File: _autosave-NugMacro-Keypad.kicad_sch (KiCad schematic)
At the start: 16 parts

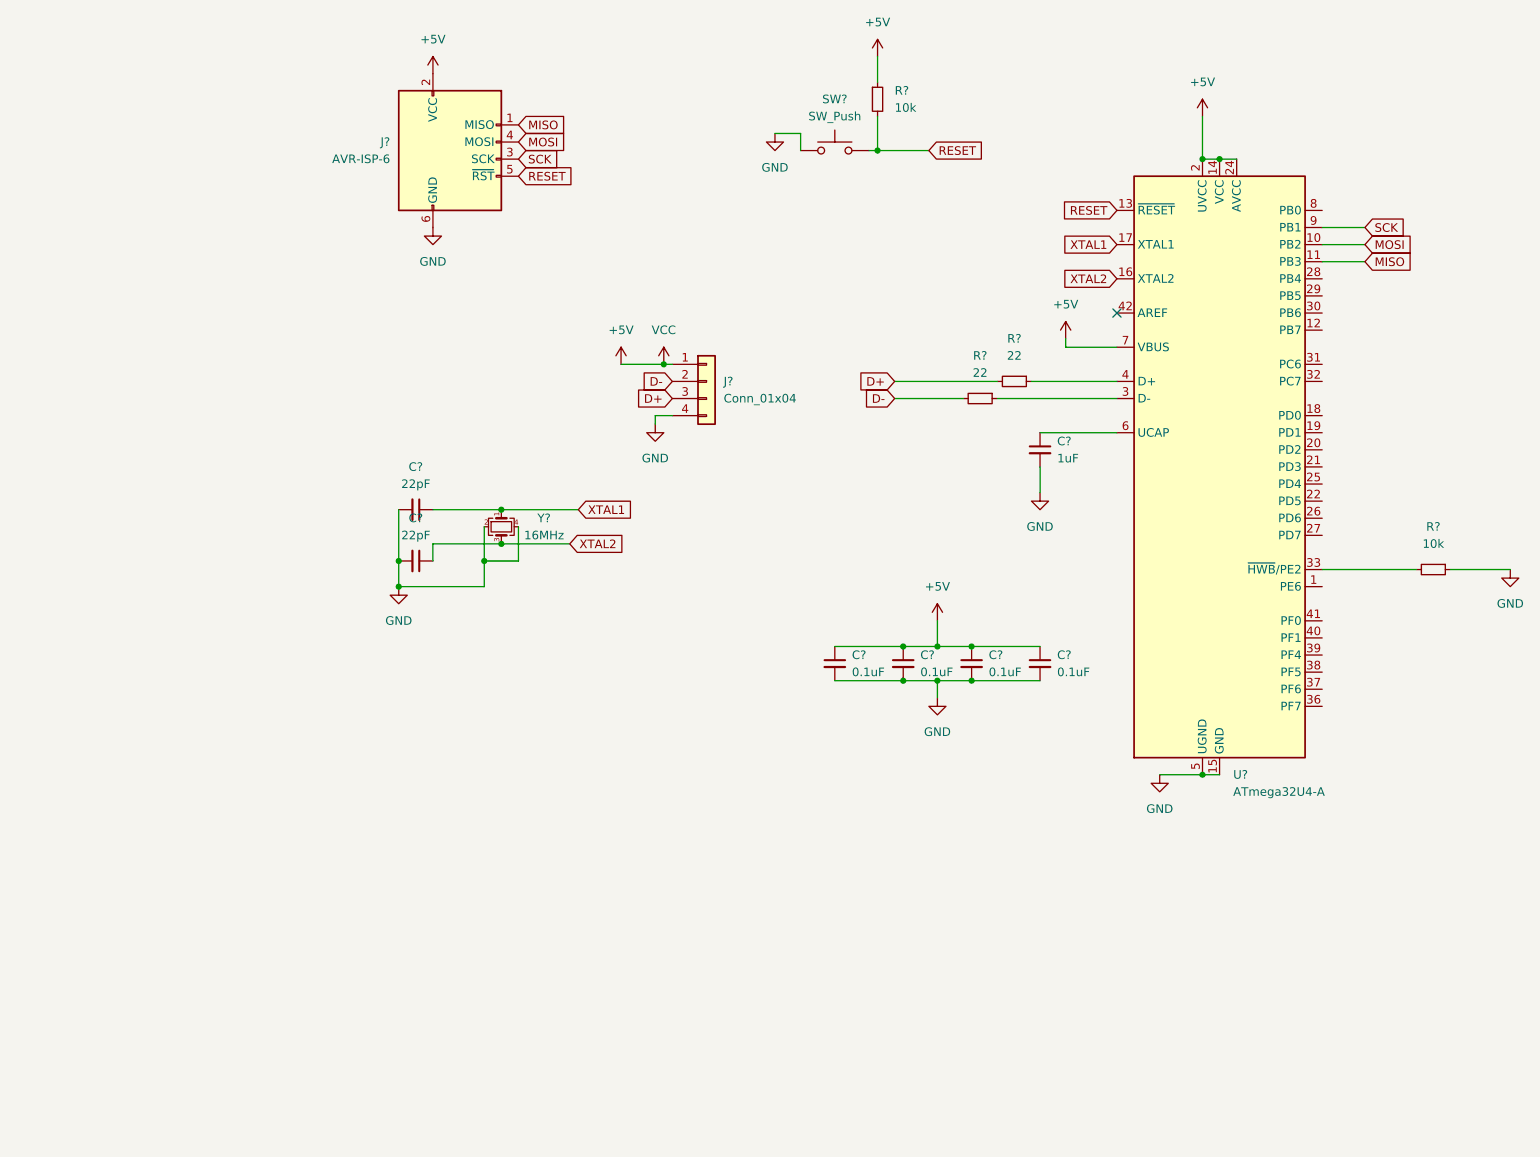
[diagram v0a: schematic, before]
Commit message: added encoder and oled with matrix
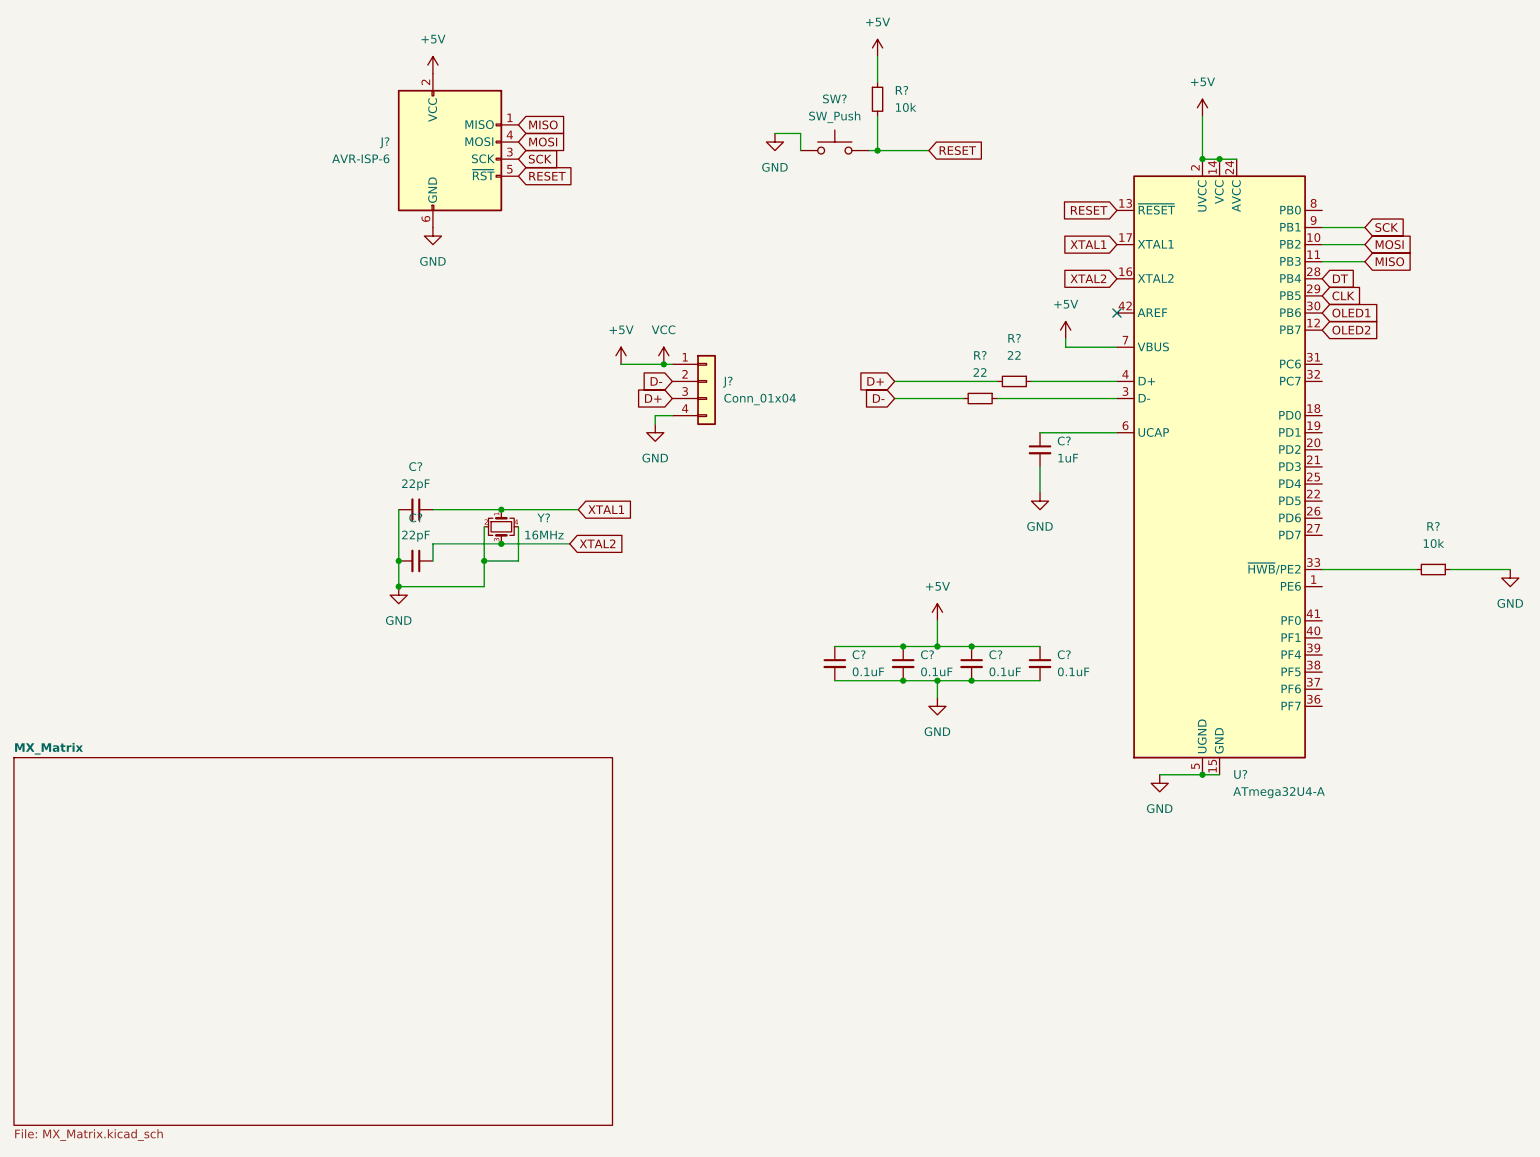
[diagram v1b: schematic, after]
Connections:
- net OLED2: now reaches U?.12 (PB7)
- net DT: now reaches U?.28 (PB4)
- net CLK: now reaches U?.29 (PB5)
- net OLED1: now reaches U?.30 (PB6)
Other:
- added sheet MX_Matrix (MX_Matrix.kicad_sch)
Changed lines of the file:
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@@
+    )
+  )
+  (global_label "DT" (shape input) (at 226.06 66.04 0) (fields_autoplaced)
+    (effects (font (size 1.27 1.27)) (justify left))
+    (property "Intersheet References" "${INTERSHEET_REFS}" (id 0) (at 230.7107 65.9606 0)
+      (effects (font (size 1.27 1.27)) (justify left) hide)
     )
   )
@@
     )
   )
+  (global_label "OLED2" (shape input) (at 226.06 73.66 0) (fields_autoplaced)
+    (effects (font (size 1.27 1.27)) (justify left))
+    (property "Intersheet References" "${INTERSHEET_REFS}" (id 0) (at 234.4602 73.5806 0)
+      (effects (font (size 1.27 1.27)) (justify left) hide)
+    )
+  )
   (global_label "XTAL1" (shape input) (at 115.57 100.33 0) (fields_autoplaced)
     (effects (font (size 1.27 1.27)) (justify left))
@@
     )
   )
+  (global_label "CLK" (shape input) (at 226.06 68.58 0) (fields_autoplaced)
+    (effects (font (size 1.27 1.27)) (justify left))
+    (property "Intersheet References" "${INTERSHEET_REFS}" (id 0) (at 232.0412 68.5006 0)
+      (effects (font (size 1.27 1.27)) (justify left) hide)
+    )
+  )
   (global_label "MISO" (shape input) (at 106.68 43.18 0) (fields_autoplaced)
     (effects (font (size 1.27 1.27)) (justify left))
@@
     (effects (font (size 1.27 1.27)) (justify left))
     (property "Intersheet References" "${INTERSHEET_REFS}" (id 0) (at 239.4193 63.4206 0)
+      (effects (font (size 1.27 1.27)) (justify left) hide)
+    )
+  )
+  (global_label "OLED1" (shape input) (at 226.06 71.12 0) (fields_autoplaced)
+    (effects (font (size 1.27 1.27)) (justify left))
+    (property "Intersheet References" "${INTERSHEET_REFS}" (id 0) (at 234.4602 71.0406 0)
       (effects (font (size 1.27 1.27)) (justify left) hide)
     )
@@
     (pin "1")
   )
+  (sheet (at 31.75 137.16) (size 88.9 54.61) (fields_autoplaced)
+    (stroke (width 0.1524) (type solid) (color 0 0 0 0))
+    (fill (color 0 0 0 0.0000))
+    (property "Sheet name" "MX_Matrix" (id 0) (at 31.75 136.4484 0)
+      (effects (font (size 1.27 1.27) bold) (justify left bottom))
+    )
+    (property "Sheet file" "MX_Matrix.kicad_sch" (id 1) (at 31.75 192.3546 0)
+      (effects (font (size 1.27 1.27)) (justify left top))
+    )
+  )
   (sheet_instances
     (path "/" (page "1"))
+    (path "/33fe6b1d-a55f-45e9-9c81-27fd5e4cace5" (page "2"))
   )
   (symbol_instances
@@
       (reference "#PWR?") (unit 1) (value "+5V") (footprint "")
     )
+    (path "/33fe6b1d-a55f-45e9-9c81-27fd5e4cace5/25fea5f4-2870-4a23-8074-22bbc9245ea4"
+      (reference "#PWR?") (unit 1) (value "+5V") (footprint "")
+    )
     (path "/309d3fc6-24a2-4977-9449-4317eec833cd"
       (reference "#PWR?") (unit 1) (value "GND") (footprint "")
@@
     )
     (path "/374c0e2a-2558-48b0-9f03-dc24c59521a6"
+      (reference "#PWR?") (unit 1) (value "GND") (footprint "")
+    )
+    (path "/33fe6b1d-a55f-45e9-9c81-27fd5e4cace5/4667430b-75ed-4f42-af10-0805cafb603d"
       (reference "#PWR?") (unit 1) (value "GND") (footprint "")
     )
@@
       (reference "#PWR?") (unit 1) (value "+5V") (footprint "")
     )
+    (path "/33fe6b1d-a55f-45e9-9c81-27fd5e4cace5/65a8e2bd-bc70-4c54-957a-8b56f5954f36"
+      (reference "#PWR?") (unit 1) (value "VCC") (footprint "")
+    )
     (path "/674d6fb6-3186-4412-a48d-fa4dfd2e106f"
       (reference "#PWR?") (unit 1) (value "GND") (footprint "")
@@
       (reference "#PWR?") (unit 1) (value "VCC") (footprint "")
     )
+    (path "/33fe6b1d-a55f-45e9-9c81-27fd5e4cace5/e388f680-1e03-4001-97c3-087fff6d0f9a"
+      (reference "#PWR?") (unit 1) (value "GND") (footprint "")
+    )
     (path "/f6c50297-e7e3-4156-8463-966e3492b299"
       (reference "#PWR?") (unit 1) (value "+5V") (footprint "")
@@
       (reference "C?") (unit 1) (value "0.1uF") (footprint "")
     )
+    (path "/33fe6b1d-a55f-45e9-9c81-27fd5e4cace5/1331d595-1d90-4299-ad1d-a0909ee78a13"
+      (reference "D?") (unit 1) (value "D_Small") (footprint "")
+    )
+    (path "/33fe6b1d-a55f-45e9-9c81-27fd5e4cace5/476218e1-ed26-4728-a036-a038631b528b"
+      (reference "D?") (unit 1) (value "D_Small") (footprint "")
+    )
+    (path "/33fe6b1d-a55f-45e9-9c81-27fd5e4cace5/481c21b9-e80f-4729-9dea-2e76899d73df"
+      (reference "D?") (unit 1) (value "D_Small") (footprint "")
+    )
+    (path "/33fe6b1d-a55f-45e9-9c81-27fd5e4cace5/4b8885a2-660e-46f0-b219-613ace276a1d"
+      (reference "D?") (unit 1) (value "D_Small") (footprint "")
+    )
+    (path "/33fe6b1d-a55f-45e9-9c81-27fd5e4cace5/50eb603f-246c-4cf1-86da-319564d2b356"
+      (reference "D?") (unit 1) (value "D_Small") (footprint "")
+    )
+    (path "/33fe6b1d-a55f-45e9-9c81-27fd5e4cace5/59ad6e03-d9f8-4f22-a095-32f25eba1474"
+      (reference "D?") (unit 1) (value "D_Small") (footprint "")
+    )
+    (path "/33fe6b1d-a55f-45e9-9c81-27fd5e4cace5/5a61f5a1-905a-46eb-8997-5e504b2efcaa"
+      (reference "D?") (unit 1) (value "D_Small") (footprint "")
+    )
+    (path "/33fe6b1d-a55f-45e9-9c81-27fd5e4cace5/65b71699-b726-42f0-846c-fab1d8beeede"
+      (reference "D?") (unit 1) (value "D_Small") (footprint "")
+    )
+    (path "/33fe6b1d-a55f-45e9-9c81-27fd5e4cace5/6cfbd7e4-bcdb-4296-94e8-be1c3436ff74"
+      (reference "D?") (unit 1) (value "D_Small") (footprint "")
+    )
+    (path "/33fe6b1d-a55f-45e9-9c81-27fd5e4cace5/947ea945-8e4a-4619-aad4-a22ebe9dd767"
+      (reference "D?") (unit 1) (value "D_Small") (footprint "")
+    )
+    (path "/33fe6b1d-a55f-45e9-9c81-27fd5e4cace5/a24f4c74-3249-4ae9-83e6-5f453da3dd60"
+      (reference "D?") (unit 1) (value "D_Small") (footprint "")
+    )
+    (path "/33fe6b1d-a55f-45e9-9c81-27fd5e4cace5/a91b5340-ec25-42e9-94b9-cb1088d5ec36"
+      (reference "D?") (unit 1) (value "D_Small") (footprint "")
+    )
+    (path "/33fe6b1d-a55f-45e9-9c81-27fd5e4cace5/d2310cf0-9fe8-4a2f-b289-29f71d05cbc1"
+      (reference "D?") (unit 1) (value "D_Small") (footprint "")
+    )
+    (path "/33fe6b1d-a55f-45e9-9c81-27fd5e4cace5/df082fe4-1f4c-4b46-9b73-980c19c04888"
+      (reference "D?") (unit 1) (value "D_Small") (footprint "")
+    )
+    (path "/33fe6b1d-a55f-45e9-9c81-27fd5e4cace5/fdf039d7-3ea7-4619-8a8c-9dfc0e958ded"
+      (reference "D?") (unit 1) (value "D_Small") (footprint "")
+    )
     (path "/000c8317-96e0-4563-8e9d-728bb31873d2"
       (reference "J?") (unit 1) (value "Conn_01x04") (footprint "")
     )
+    (path "/33fe6b1d-a55f-45e9-9c81-27fd5e4cace5/6d630448-4c55-4782-8b84-801fff5d4d9f"
+      (reference "J?") (unit 1) (value "Conn_01x04_Female_For_LCD") (footprint "")
+    )
     (path "/7889a702-8281-40f8-bfaa-98c3ed2535eb"
       (reference "J?") (unit 1) (value "AVR-ISP-6") (footprint "")
     )
+    (path "/33fe6b1d-a55f-45e9-9c81-27fd5e4cace5/05ddfc09-b6c2-4ebd-ae6b-99d4339be5d1"
+      (reference "MX?") (unit 1) (value "MX-NoLED") (footprint "")
+    )
+    (path "/33fe6b1d-a55f-45e9-9c81-27fd5e4cace5/1d6be2a6-be28-45c8-ae25-50d4012f8abc"
+      (reference "MX?") (unit 1) (value "MX-NoLED") (footprint "")
+    )
+    (path "/33fe6b1d-a55f-45e9-9c81-27fd5e4cace5/204d3d72-00bb-424e-b63b-8747019a7f38"
+      (reference "MX?") (unit 1) (value "MX-NoLED") (footprint "")
+    )
+    (path "/33fe6b1d-a55f-45e9-9c81-27fd5e4cace5/216689ee-2493-4584-b54e-685748062766"
+      (reference "MX?") (unit 1) (value "MX-NoLED") (footprint "")
+    )
+    (path "/33fe6b1d-a55f-45e9-9c81-27fd5e4cace5/27a79e30-d521-4065-94a3-01d68fefeb9f"
+      (reference "MX?") (unit 1) (value "MX-NoLED") (footprint "")
+    )
+    (path "/33fe6b1d-a55f-45e9-9c81-27fd5e4cace5/351c0988-f141-4020-90ab-933a3415d3d6"
+      (reference "MX?") (unit 1) (value "MX-NoLED") (footprint "")
+    )
+    (path "/33fe6b1d-a55f-45e9-9c81-27fd5e4cace5/373448e3-6e93-44f8-8773-73d32d8623c9"
+      (reference "MX?") (unit 1) (value "MX-NoLED") (footprint "")
+    )
+    (path "/33fe6b1d-a55f-45e9-9c81-27fd5e4cace5/4627e8c3-0641-4dbe-ba3b-5a486218d1de"
+      (reference "MX?") (unit 1) (value "MX-NoLED") (footprint "")
+    )
+    (path "/33fe6b1d-a55f-45e9-9c81-27fd5e4cace5/4d709a7f-57b4-41dd-a92e-5837f865b4df"
+      (reference "MX?") (unit 1) (value "MX-NoLED") (footprint "")
+    )
+    (path "/33fe6b1d-a55f-45e9-9c81-27fd5e4cace5/62e38145-3ad1-4b60-8412-e9e25730017a"
+      (reference "MX?") (unit 1) (value "MX-NoLED") (footprint "")
+    )
+    (path "/33fe6b1d-a55f-45e9-9c81-27fd5e4cace5/7d5e9834-61a5-462b-890c-5e4eae09f56e"
+      (reference "MX?") (unit 1) (value "MX-NoLED") (footprint "")
+    )
+    (path "/33fe6b1d-a55f-45e9-9c81-27fd5e4cace5/8bf6aa70-d00c-4090-83da-5a7b598adb41"
+      (reference "MX?") (unit 1) (value "MX-NoLED") (footprint "")
+    )
+    (path "/33fe6b1d-a55f-45e9-9c81-27fd5e4cace5/a1cfc593-b67b-4742-8080-24c93873bf23"
+      (reference "MX?") (unit 1) (value "MX-NoLED") (footprint "")
+    )
+    (path "/33fe6b1d-a55f-45e9-9c81-27fd5e4cace5/c3a9b996-0159-4cc3-91eb-d30875d5a676"
+      (reference "MX?") (unit 1) (value "MX-NoLED") (footprint "")
+    )
+    (path "/33fe6b1d-a55f-45e9-9c81-27fd5e4cace5/e8922759-5f60-48fe-83e0-7609591d3cfa"
+      (reference "MX?") (unit 1) (value "MX-NoLED") (footprint "")
+    )
     (path "/4ca06591-1cd5-439b-bf8b-2a0c92e44b1f"
       (reference "R?") (unit 1) (value "10k") (footprint "")
@@
       (reference "R?") (unit 1) (value "22") (footprint "")
     )
+    (path "/33fe6b1d-a55f-45e9-9c81-27fd5e4cace5/eadd7d6a-dd96-41e2-b6a7-47c774bfc85f"
+      (reference "R?") (unit 1) (value "10K") (footprint "")
+    )
+    (path "/33fe6b1d-a55f-45e9-9c81-27fd5e4cace5/f6497caa-a790-4fab-afa9-23395e924b4e"
+      (reference "R?") (unit 1) (value "10K") (footprint "")
+    )
+    (path "/33fe6b1d-a55f-45e9-9c81-27fd5e4cace5/14e7f223-a164-442d-9c5e-9995ebfe5b72"
+      (reference "SW?") (unit 1) (value "RotaryEncoder_Switch") (footprint "")
+    )
     (path "/a573fc8f-1b31-460e-bddf-15f8e483f9e1"
